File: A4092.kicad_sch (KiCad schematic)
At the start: 0 parts

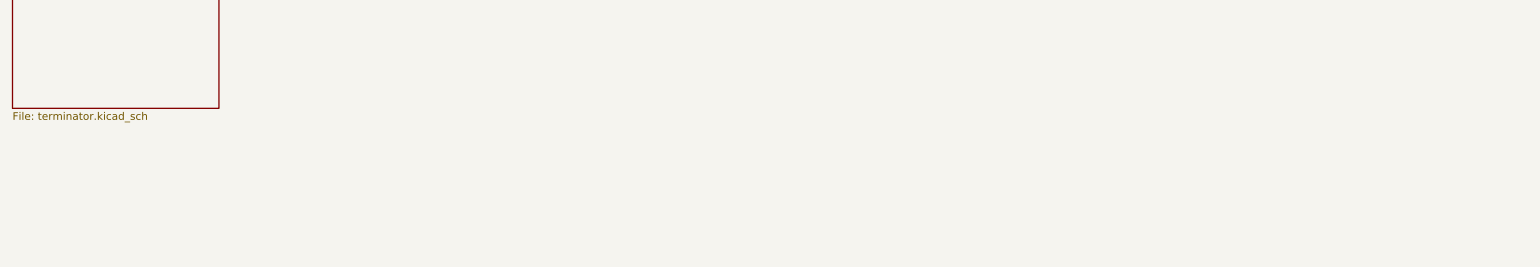
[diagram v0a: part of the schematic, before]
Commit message: Start populating Zorro III
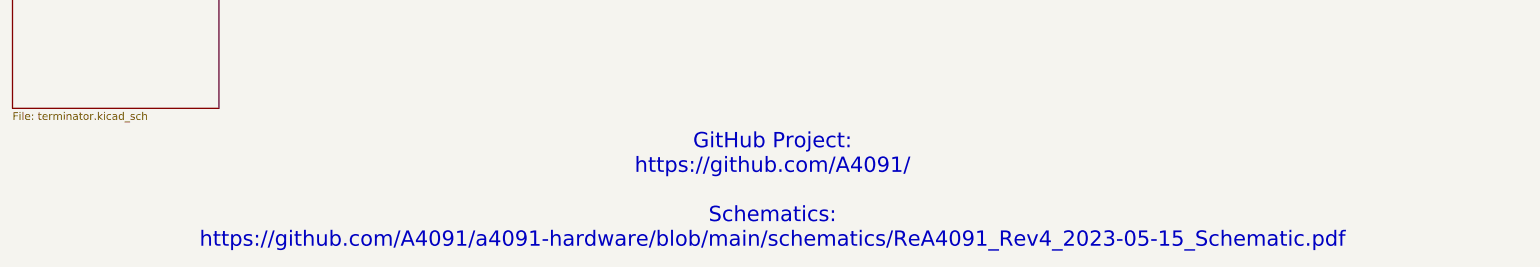
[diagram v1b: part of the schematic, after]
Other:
- note added: "GitHub Project: https://github.com/A4091/ Schematics: https://github.com/A4091/a4091-hardware/blob/main/schematics/ReA4091_Rev4_2023-05-15_Schematic.pdf"
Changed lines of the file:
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@@
 	(generator_version "9.0")
 	(paper "A4")
+	(text "GitHub Project:\nhttps://github.com/A4091/\n\nSchematics:\nhttps://github.com/A4091/a4091-hardware/blob/main/schematics/ReA4091_Rev4_2023-05-15_Schematic.pdf"
+		(exclude_from_sim no)
+		(at 151.638 110.236 0)
+		(effects
+			(font
+				(size 2.54 2.54)
+			)
+		)
+	)
 	(sheet
 		(at 222.25 25.4)

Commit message: Update design
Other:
- note added: "Commodore A4091 Rev B Advanced SCSI II Controller Board This Zorro III board was originally designed and sold by Commodore, which did a single run of the Rev A design before shelving it. Commodore was running out of money at the time and didn't want to risk a second production run. The Rev B design was given to DKB Software for production, marketing, sales, distribution, and support. Features: 􂀢 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"
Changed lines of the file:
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@@
 	(generator_version "9.0")
 	(paper "A4")
+	(text "Commodore A4091\nRev B Advanced SCSI II Controller Board\nThis Zorro III board was originally designed and sold by Commodore, which did a single\nrun of the Rev A design before shelving it. Commodore was running out of money at the\ntime and didn't want to risk a second production run. The Rev B design was given to\nDKB Software for production, marketing, sales, distribution, and support.\nFeatures:\n􂀢 Boot ROM\n􂀢 NCR 53C710 SCSI II controller\n􂀢 50 pin internal connector\n􂀢 50 pin external SCSI2 connector\n􂀢 3.5\" hard drive mounts on the card\n􂀢 Active SCSI termination\n􂀢 Zorro III bus support\nCaveats:\n􂀢 Requires Buster 11\n􂀢 Does not work with with A3640 Rev 3.0\n􂀢 No RAM option\n􂀢 No wide SCSI support\nThe Commodore A4091 was reverse-engineered by Stefan Reinauer and Chris Hooper."
+		(exclude_from_sim no)
+		(at 89.916 155.448 0)
+		(effects
+			(font
+				(size 1.27 1.27)
+			)
+		)
+	)
 	(text "GitHub Project:\nhttps://github.com/A4091/\n\nSchematics:\nhttps://github.com/A4091/a4091-hardware/blob/main/schematics/ReA4091_Rev4_2023-05-15_Schematic.pdf"
 		(exclude_from_sim no)

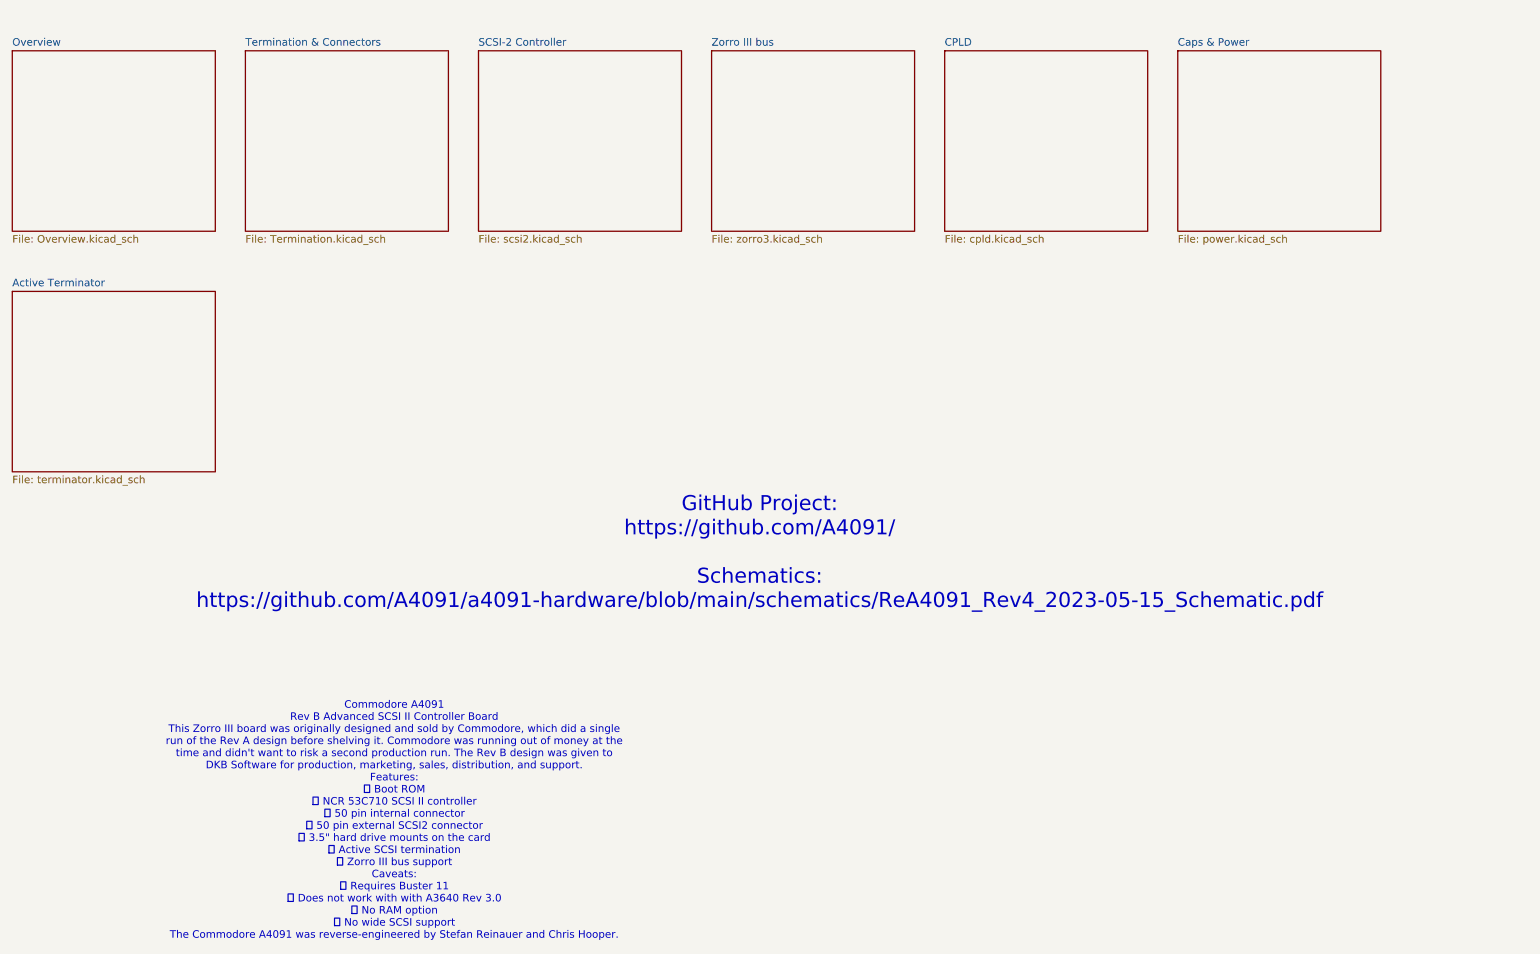
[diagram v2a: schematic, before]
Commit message: Redraw footprints, finish Termination/Connectors
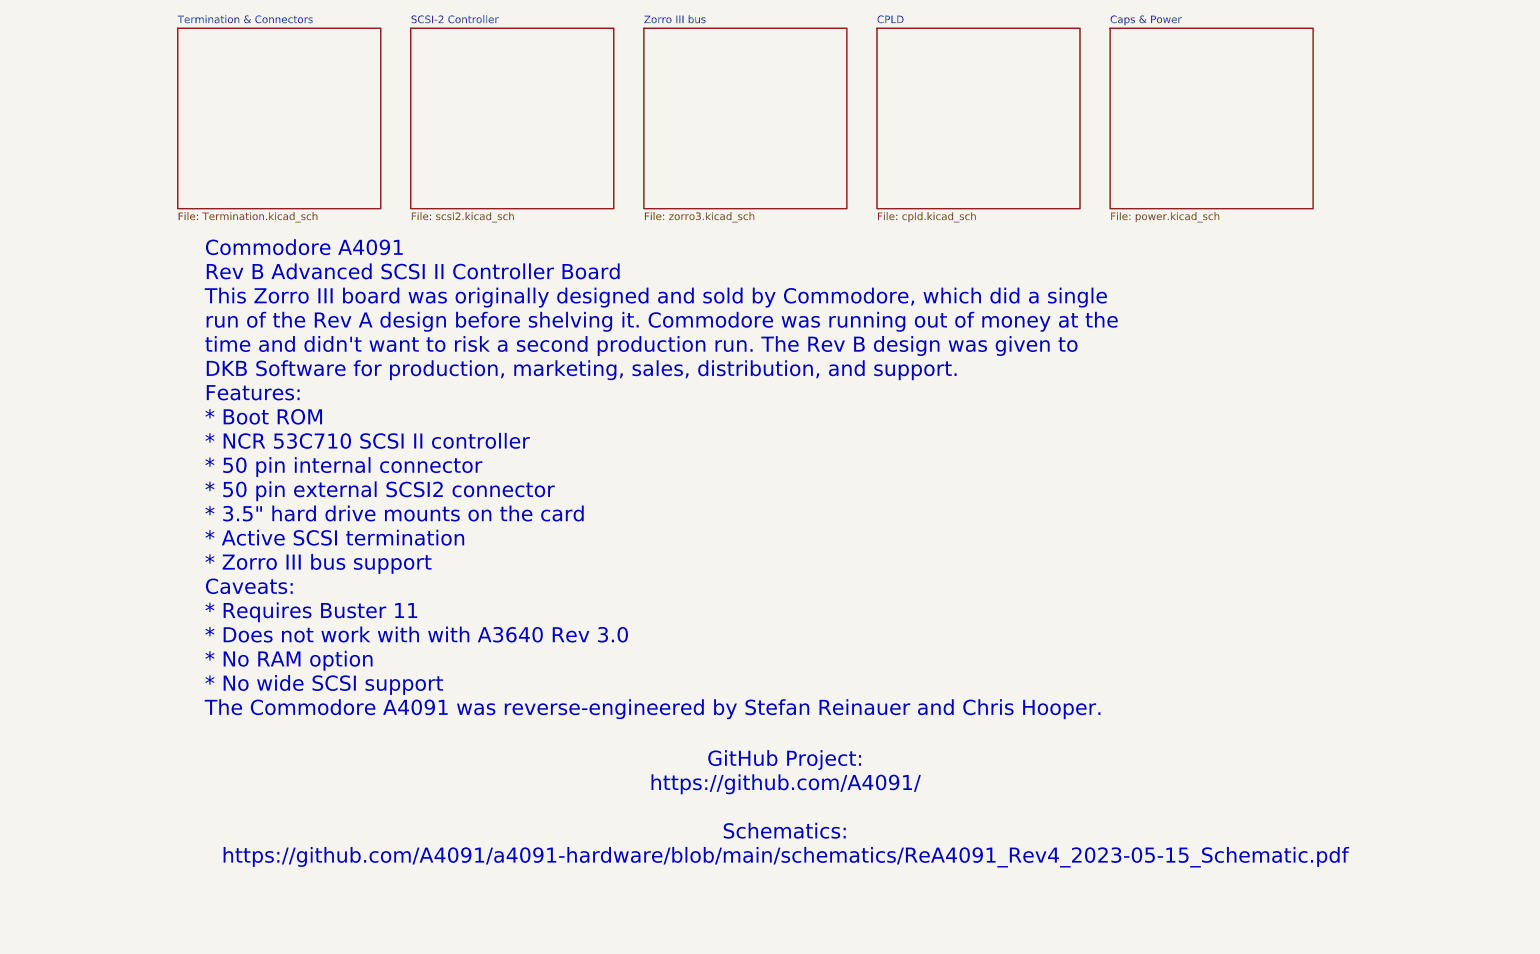
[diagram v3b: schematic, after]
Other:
- removed sheet Active Terminator
- removed sheet Overview
- note added: "Commodore A4091 Rev B Advanced SCSI II Controller Board This Zorro III board was originally designed and sold by Commodore, which did a single run of the Rev A design before shelving it. Commodore was running out of money at the time and didn't want to risk a second production run. The Rev B design was given to DKB Software for production, marketing, sales, distribution, and support. Features: * 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"
- note removed: "Commodore A4091 Rev B Advanced SCSI II Controller Board This Zorro III board was originally designed and sold by Commodore, which did a single run of the Rev A design before shelving it. Commodore was running out of money at the time and didn't want to risk a second production run. The Rev B design was given to DKB Software for production, marketing, sales, distribution, and support. Features: 􂀢 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"
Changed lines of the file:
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@@
 	(generator_version "9.0")
 	(paper "A4")
-	(text "Commodore A4091\nRev B Advanced SCSI II Controller Board\nThis Zorro III board was originally designed and sold by Commodore, which did a single\nrun of the Rev A design before shelving it. Commodore was running out of money at the\ntime and didn't want to risk a second production run. The Rev B design was given to\nDKB Software for production, marketing, sales, distribution, and support.\nFeatures:\n􂀢 Boot ROM\n􂀢 NCR 53C710 SCSI II controller\n􂀢 50 pin internal connector\n􂀢 50 pin external SCSI2 connector\n􂀢 3.5\" hard drive mounts on the card\n􂀢 Active SCSI termination\n􂀢 Zorro III bus support\nCaveats:\n􂀢 Requires Buster 11\n􂀢 Does not work with with A3640 Rev 3.0\n􂀢 No RAM option\n􂀢 No wide SCSI support\nThe Commodore A4091 was reverse-engineered by Stefan Reinauer and Chris Hooper."
-		(exclude_from_sim no)
-		(at 89.916 155.448 0)
-		(effects
-			(font
-				(size 1.27 1.27)
-			)
-		)
-	)
-	(text "GitHub Project:\nhttps://github.com/A4091/\n\nSchematics:\nhttps://github.com/A4091/a4091-hardware/blob/main/schematics/ReA4091_Rev4_2023-05-15_Schematic.pdf"
-		(exclude_from_sim no)
-		(at 151.638 110.236 0)
+	(text "Commodore A4091\nRev B Advanced SCSI II Controller Board\nThis Zorro III board was originally designed and sold by Commodore, which did a single\nrun of the Rev A design before shelving it. Commodore was running out of money at the\ntime and didn't want to risk a second production run. The Rev B design was given to\nDKB Software for production, marketing, sales, distribution, and support.\nFeatures:\n* Boot ROM\n* NCR 53C710 SCSI II controller\n* 50 pin internal connector\n* 50 pin external SCSI2 connector\n* 3.5\" hard drive mounts on the card\n* Active SCSI termination\n* Zorro III bus support\nCaveats:\n* Requires Buster 11\n* Does not work with with A3640 Rev 3.0\n* No RAM option\n* No wide SCSI support\nThe Commodore A4091 was reverse-engineered by Stefan Reinauer and Chris Hooper."
+		(exclude_from_sim no)
+		(at 57.912 97.79 0)
 		(effects
 			(font
 				(size 2.54 2.54)
 			)
-		)
-	)
-	(sheet
-		(at 222.25 25.4)
+			(justify left)
+		)
+	)
+	(text "GitHub Project:\nhttps://github.com/A4091/\n\nSchematics:\nhttps://github.com/A4091/a4091-hardware/blob/main/schematics/ReA4091_Rev4_2023-05-15_Schematic.pdf"
+		(exclude_from_sim no)
+		(at 155.956 153.416 0)
+		(effects
+			(font
+				(size 2.54 2.54)
+			)
+		)
+	)
+	(sheet
+		(at 210.82 21.59)
 		(size 34.29 30.48)
 		(exclude_from_sim no)
@@
 		)
 		(property "Sheetname" "Caps & Power"
-			(at 222.25 24.6884 0)
+			(at 210.82 20.8784 0)
 			(effects
 				(font
@@
 		)
 		(property "Sheetfile" "power.kicad_sch"
-			(at 222.25 56.4646 0)
+			(at 210.82 52.6546 0)
 			(effects
 				(font
@@
 	)
 	(sheet
-		(at 104.14 25.4)
+		(at 92.71 21.59)
 		(size 34.29 30.48)
 		(exclude_from_sim no)
@@
 		)
 		(property "Sheetname" "SCSI-2 Controller"
-			(at 104.14 24.6884 0)
+			(at 92.71 20.8784 0)
 			(effects
 				(font
@@
 		)
 		(property "Sheetfile" "scsi2.kicad_sch"
-			(at 104.14 56.4646 0)
+			(at 92.71 52.6546 0)
 			(effects
 				(font
@@
 	)
 	(sheet
-		(at 64.77 25.4)
+		(at 53.34 21.59)
 		(size 34.29 30.48)
 		(exclude_from_sim no)
@@
 		)
 		(property "Sheetname" "Termination & Connectors"
-			(at 64.77 24.6884 0)
+			(at 53.34 20.8784 0)
 			(effects
 				(font
@@
 		)
 		(property "Sheetfile" "Termination.kicad_sch"
-			(at 64.77 56.4646 0)
+			(at 53.34 52.6546 0)
 			(effects
 				(font
@@
 	)
 	(sheet
-		(at 143.51 25.4)
+		(at 132.08 21.59)
 		(size 34.29 30.48)
 		(exclude_from_sim no)
@@
 		)
 		(property "Sheetname" "Zorro III bus"
-			(at 143.51 24.6884 0)
+			(at 132.08 20.8784 0)
 			(effects
 				(font
@@
 		)
 		(property "Sheetfile" "zorro3.kicad_sch"
-			(at 143.51 56.4646 0)
+			(at 132.08 52.6546 0)
 			(effects
 				(font
@@
 	)
 	(sheet
-		(at 182.88 25.4)
+		(at 171.45 21.59)
 		(size 34.29 30.48)
 		(exclude_from_sim no)
@@
 		)
 		(property "Sheetname" "CPLD"
-			(at 182.88 24.6884 0)
+			(at 171.45 20.8784 0)
 			(effects
 				(font
@@
 		)
 		(property "Sheetfile" "cpld.kicad_sch"
-			(at 182.88 56.4646 0)
+			(at 171.45 52.6546 0)
 			(effects
 				(font
@@
 				)
 			)
-		)
-	)
-	(sheet
-		(at 25.4 25.4)
-		(size 34.29 30.48)
-		(exclude_from_sim no)
-		(in_bom yes)
-		(on_board yes)
-		(dnp no)
-		(fields_autoplaced yes)
-		(stroke
-			(width 0.1524)
-			(type solid)
-		)
-		(fill
-			(color 0 0 0 0.0000)
-		)
-		(property "Sheetname" "Overview"
-			(at 25.4 24.6884 0)
-			(show_name yes)
-			(effects
-				(font
-					(size 1.27 1.27)
-				)
-				(justify left bottom)
-			)
-		)
-		(property "Sheetfile" "Overview.kicad_sch"
-			(at 25.4 56.4646 0)
-			(effects
-				(font
-					(size 1.27 1.27)
-				)
-				(justify left top)
-			)
-		)
-		(instances
-			(project "A4092"
-				(path "/8f9f4021-47aa-41d9-bea7-f6ccf72098bb"
-					(page "2")
-				)
-			)
-		)
-	)
-	(sheet
-		(at 25.4 66.04)
-		(size 34.29 30.48)
-		(exclude_from_sim no)
-		(in_bom yes)
-		(on_board yes)
-		(dnp no)
-		(fields_autoplaced yes)
-		(stroke
-			(width 0.1524)
-			(type solid)
-		)
-		(fill
-			(color 0 0 0 0.0000)
-		)
-		(property "Sheetname" "Active Terminator"
-			(at 25.4 65.3284 0)
-			(effects
-				(font
-					(size 1.27 1.27)
-				)
-				(justify left bottom)
-			)
-		)
-		(property "Sheetfile" "terminator.kicad_sch"
-			(at 25.4 97.1046 0)
-			(effects
-				(font
-					(size 1.27 1.27)
-				)
-				(justify left top)
-			)
-		)
-		(instances
-			(project "A4092"
-				(path "/8f9f4021-47aa-41d9-bea7-f6ccf72098bb"
-					(page "8")
-				)
-			)
